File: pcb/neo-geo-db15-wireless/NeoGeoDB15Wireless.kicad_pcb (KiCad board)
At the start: 2 copper layers, 3 parts, among them J1 DB15_Female_MountingHoles, U1 RP2040-Zero, U2 NRF24L01_Breakout

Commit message: PCB schematic
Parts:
- U2: moved to B.Cu
- moved U2 29.5 mm to (113.0, 72.0), turned to 180 degrees
- moved J1 29.1 mm to (100.0, 92.8), turned to 180 degrees
- moved U1 19.5 mm to (104.6, 82.2), turned to 90 degrees
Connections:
- J1 pad 1: unconnected-(J1-Pad1) -> /GND
- J1 pad 11: unconnected-(J1-Pad11) -> /STA
- J1 pad 12: unconnected-(J1-Pad12) -> /BC
- J1 pad 13: unconnected-(J1-Pad13) -> /BA
- J1 pad 14: unconnected-(J1-Pad14) -> /DL
- J1 pad 15: unconnected-(J1-Pad15) -> /DU
- J1 pad 3: unconnected-(J1-Pad3) -> /SEL
- J1 pad 4: unconnected-(J1-Pad4) -> /BD
- J1 pad 5: unconnected-(J1-Pad5) -> /BB
- J1 pad 6: unconnected-(J1-Pad6) -> /DR
- J1 pad 7: unconnected-(J1-Pad7) -> /DD
- J1 pad 8: unconnected-(J1-Pad8) -> /VCC
- U1 pad 1: unconnected-(U1-Pad1) -> /DU
- U1 pad 10: unconnected-(U1-Pad10) -> /SEL
- U1 pad 13: unconnected-(U1-Pad13) -> /MISO
- U1 pad 14: unconnected-(U1-Pad14) -> /CS
- U1 pad 15: unconnected-(U1-Pad15) -> /SCK
- U1 pad 16: unconnected-(U1-Pad16) -> /MOSI
- U1 pad 17: unconnected-(U1-Pad17) -> /CE
- U1 pad 18: unconnected-(U1-Pad18) -> /IRQ
- U1 pad 19: Net-(U1-Pad19) -> unconnected-(U1-Pad19)
- U1 pad 2: unconnected-(U1-Pad2) -> /DD
- U1 pad 20: Net-(U1-Pad20) -> unconnected-(U1-Pad20)
- U1 pad 21: unconnected-(U1-Pad21) -> Net-(U1-Pad21)
- U1 pad 22: unconnected-(U1-Pad22) -> /VCC
- U1 pad 23: unconnected-(U1-Pad23) -> /GND
- U1 pad 3: unconnected-(U1-Pad3) -> /DL
- U1 pad 4: unconnected-(U1-Pad4) -> /DR
- U1 pad 5: unconnected-(U1-Pad5) -> /BA
- U1 pad 6: unconnected-(U1-Pad6) -> /BB
- U1 pad 7: unconnected-(U1-Pad7) -> /BC
- U1 pad 8: unconnected-(U1-Pad8) -> /BD
- U1 pad 9: unconnected-(U1-Pad9) -> /STA
- U2 pad 1: unconnected-(U2-Pad1) -> /GND
- U2 pad 2: unconnected-(U2-Pad2) -> Net-(U1-Pad21)
- U2 pad 3: Net-(U1-Pad20) -> /CE
- U2 pad 4: unconnected-(U2-Pad4) -> /CS
- U2 pad 5: unconnected-(U2-Pad5) -> /SCK
- U2 pad 6: unconnected-(U2-Pad6) -> /MOSI
- U2 pad 7: unconnected-(U2-Pad7) -> /MISO
- U2 pad 8: Net-(U1-Pad19) -> /IRQ
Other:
- board outline added: 40 x 41 mm

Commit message: Routing
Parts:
- moved U2 0.71 mm to (112.5, 72.5), turned to 0 degrees
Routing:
- net /IRQ: track 0.00 -> 40.6 mm
- net /MOSI: track 0.00 -> 32.6 mm
- net /BC: track 0.00 -> 31.0 mm
- net /STA: track 0.00 -> 29.3 mm
- net /DU: track 0.00 -> 28.2 mm
- net /DD: track 0.00 -> 27.9 mm
- net Net-(U1-Pad21): track 0.00 -> 27.8 mm
- net /BD: track 0.00 -> 26.8 mm
- net /DL: track 0.00 -> 26.6 mm
- net /BA: track 0.00 -> 26.5 mm
- net /BB: track 0.00 -> 24.1 mm
- net /SCK: track 0.00 -> 23.6 mm
- net /CE: track 0.00 -> 23.3 mm
- net /DR: track 0.00 -> 23.3 mm
- net /SEL: track 0.00 -> 22.4 mm
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- added copper zone on B.Cu, net /GND
- added copper zone on F.Cu, net /GND

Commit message: Making the right size
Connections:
- net Net-(U1-Pad21) renamed /3V3
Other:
- board size 40 x 41 mm -> 39.9 x 29.2 mm
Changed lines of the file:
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@@
       (outputformat 1)
       (mirror false)
-      (drillshape 1)
+      (drillshape 0)
       (scaleselection 1)
-      (outputdirectory "")
+      (outputdirectory "Gerbers/")
     )
   )
@@
   (net 22 "unconnected-(U1-Pad19)")
   (net 23 "unconnected-(U1-Pad20)")
-  (net 24 "Net-(U1-Pad21)")
+  (net 24 "/3V3")
   (net 25 "unconnected-(U1-Pad11)")
   (net 26 "unconnected-(U1-Pad12)")
@@
       (effects (font (size 1 1) (thickness 0.15)))
     )
-    (fp_line (start 19.16 -0.95) (end 19.16 -24.45) (layer "F.SilkS") (width 0.12))
-    (fp_line (start 1.16 -0.95) (end 19.16 -0.95) (layer "F.SilkS") (width 0.12))
-    (fp_line (start 19.16 -24.45) (end 1.16 -24.45) (layer "F.SilkS") (width 0.12))
-    (fp_line (start 1.16 -24.45) (end 1.16 -0.95) (layer "F.SilkS") (width 0.12))
     (fp_line (start 1.16 -0.95) (end 1.16 -24.45) (layer "F.CrtYd") (width 0.05))
     (fp_line (start 19.16 -0.95) (end 1.16 -0.95) (layer "F.CrtYd") (width 0.05))
@@
       (net 23 "unconnected-(U1-Pad20)") (pinfunction "GP29") (pintype "bidirectional+no_connect"))
     (pad "21" thru_hole roundrect (at 2.54 -17.78 90) (size 2.6 1.6002) (drill 0.8 (offset -0.6 0)) (layers *.Cu *.Mask) (roundrect_rratio 0.25)
-      (net 24 "Net-(U1-Pad21)") (pinfunction "3V3") (pintype "power_in"))
+      (net 24 "/3V3") (pinfunction "3V3") (pintype "power_in"))
     (pad "22" thru_hole roundrect (at 2.54 -12.7 90) (size 2.6 1.6002) (drill 0.8 (offset -0.6 0)) (layers *.Cu *.Mask) (roundrect_rratio 0.25)
       (net 3 "/VCC") (pinfunction "5V") (pintype "power_in"))
@@
     (property "Sheetname" "")
     (attr through_hole)
-    (fp_text reference "J1" (at -21.1709 8.1408 180) (layer "F.SilkS")
+    (fp_text reference "J1" (at 0.8 0.25 180) (layer "F.SilkS") hide
       (effects (font (size 1 1) (thickness 0.15)) (justify left))
     )
@@
       (effects (font (size 1.27 1.27) (thickness 0.15)))
     )
-    (fp_text user "Connector out this way" (at 0 -6 unlocked) (layer "F.SilkS")
-      (effects (font (size 1 1) (thickness 0.15)))
-    )
-    (fp_line (start 19.7612 9.5885) (end 19.7612 -9.5885) (layer "F.SilkS") (width 0.15))
-    (fp_line (start -19.7612 9.5885) (end 19.7612 9.5885) (layer "F.SilkS") (width 0.15))
-    (fp_line (start -19.7612 9.5885) (end -19.7612 -9.5885) (layer "F.SilkS") (width 0.15))
-    (fp_line (start -19.7612 -9.5885) (end 19.7612 -9.5885) (layer "F.SilkS") (width 0.15))
-    (fp_rect (start -16 -9.5885) (end 16 -2) (layer "F.SilkS") (width 0.12) (fill none))
-    (fp_poly (pts
-        (xy 1 -8)
-        (xy -1 -8)
-        (xy 0 -9)
-      ) (layer "F.SilkS") (width 0.12) (fill solid))
     (fp_line (start -19.7862 9.6135) (end 19.7862 9.6135) (layer "F.CrtYd") (width 0.15))
     (fp_line (start 19.7862 9.6135) (end 19.7862 -9.6135) (layer "F.CrtYd") (width 0.15))
@@
     (fp_line (start -19.7612 -9.5885) (end 19.7612 -9.5885) (layer "F.Fab") (width 0.15))
     (fp_line (start -19.7612 9.5885) (end -19.7612 -9.5885) (layer "F.Fab") (width 0.15))
-    (pad "" np_thru_hole circle (at -16.6624 6.2992 180) (size 4.825 4.825) (drill 3.175) (layers F&B.Cu *.Mask)
-      (pinfunction "PAD") (pintype "passive+no_connect"))
-    (pad "" np_thru_hole circle (at 16.6624 6.2992 180) (size 4.825 4.825) (drill 3.175) (layers F&B.Cu *.Mask)
-      (pinfunction "PAD") (pintype "passive+no_connect"))
+    (pad "" np_thru_hole circle (at -16.6624 6.2992 180) (size 4.825 4.825) (drill 3.175) (layers F&B.Cu *.Mask))
+    (pad "" np_thru_hole circle (at 16.6624 6.2992 180) (size 4.825 4.825) (drill 3.175) (layers F&B.Cu *.Mask))
     (pad "1" thru_hole circle (at -9.601192 7.7216 180) (size 1.591397 1.591397) (drill 1.0414) (layers *.Cu *.Mask)
       (net 10 "/GND") (pinfunction "1") (pintype "passive"))
@@
       (net 10 "/GND") (pinfunction "GND") (pintype "power_in"))
     (pad "2" smd rect (at -4.4 -8.7) (size 1 2) (layers "B.Cu" "B.Paste" "B.Mask")
-      (net 24 "Net-(U1-Pad21)") (pinfunction "VCC") (pintype "power_in"))
+      (net 24 "/3V3") (pinfunction "VCC") (pintype "power_in"))
     (pad "3" smd rect (at -1.86 -8.7) (size 1 2) (layers "B.Cu" "B.Paste" "B.Mask")
       (net 20 "/CE") (pinfunction "CE") (pintype "input"))
@@
     )
   )
-  (gr_rect (start 80 102.5) (end 120 61.5) (layer "Edge.Cuts") (width 0.1) (fill none))
+  (gr_rect (start 80 90.7) (end 119.9 61.5) (layer "Edge.Cuts") (width 0.1) (fill none))
   (segment (start 90.398799 85.0284) (end 91.925 83.502199) (width 0.4) (layer "F.Cu") (net 3))
   (segment (start 91.925 83.502199) (end 91.925 79.675) (width 0.4) (layer "F.Cu") (net 3))
@@
   (segment (start 97.25 83.25) (end 94.465 80.465) (width 0.25) (layer "B.Cu") (net 21))
   (segment (start 111.25 83.25) (end 97.25 83.25) (width 0.25) (layer "B.Cu") (net 21))
-  (segment (start 101.06 65.46) (end 86.845 79.675) (width 0.25) (layer "B.Cu") (net 24))
-  (segment (start 106.44 65.46) (end 101.06 65.46) (width 0.25) (layer "B.Cu") (net 24))
-  (segment (start 108.1 63.8) (end 106.44 65.46) (width 0.25) (layer "B.Cu") (net 24))
+  (segment (start 106.3 65.6) (end 108.1 63.8) (width 0.4) (layer "B.Cu") (net 24))
+  (segment (start 86.845 79.655) (end 100.9 65.6) (width 0.4) (layer "B.Cu") (net 24))
+  (segment (start 86.845 79.675) (end 86.845 79.655) (width 0.4) (layer "B.Cu") (net 24))
+  (segment (start 100.9 65.6) (end 106.3 65.6) (width 0.4) (layer "B.Cu") (net 24))
   (zone (net 10) (net_name "/GND") (layers F&B.Cu) (hatch edge 0.508)
     (connect_pads (clearance 0.508))

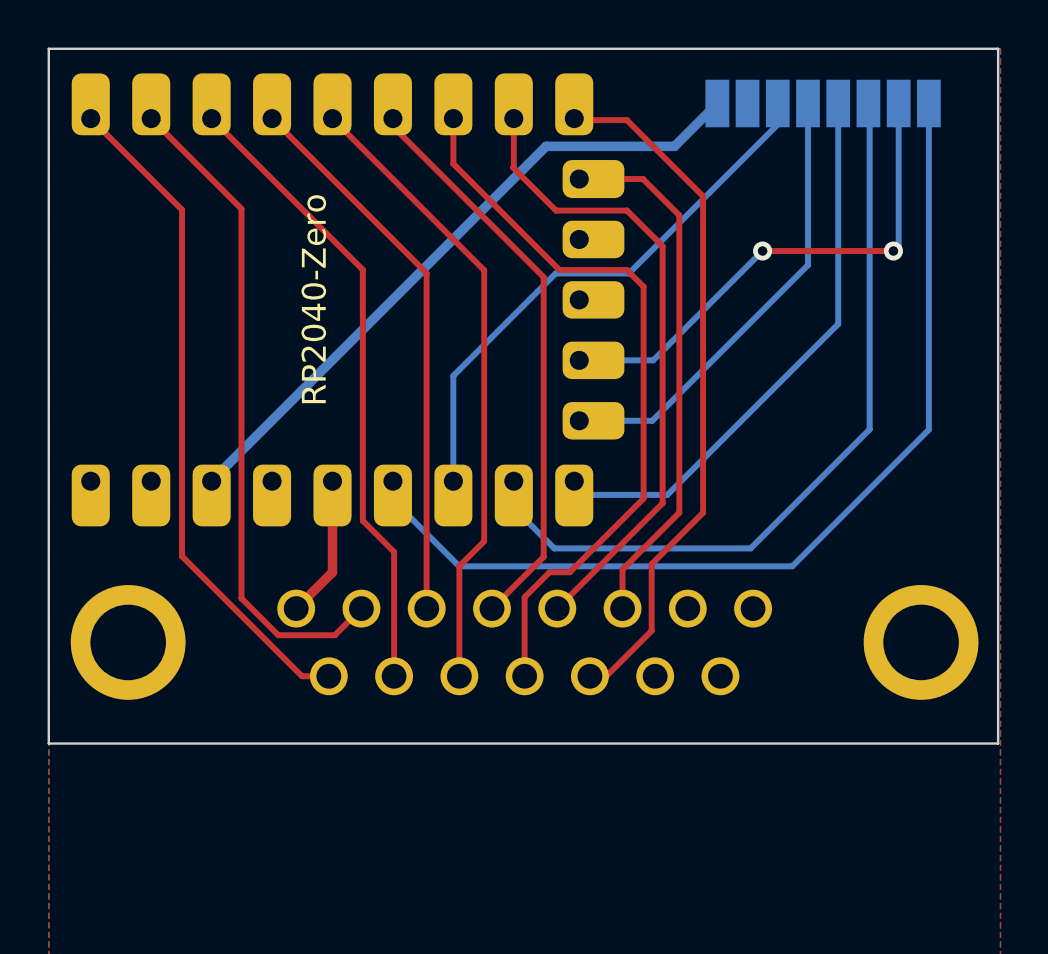
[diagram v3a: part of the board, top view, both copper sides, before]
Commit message: Correct size, add some silkscreen
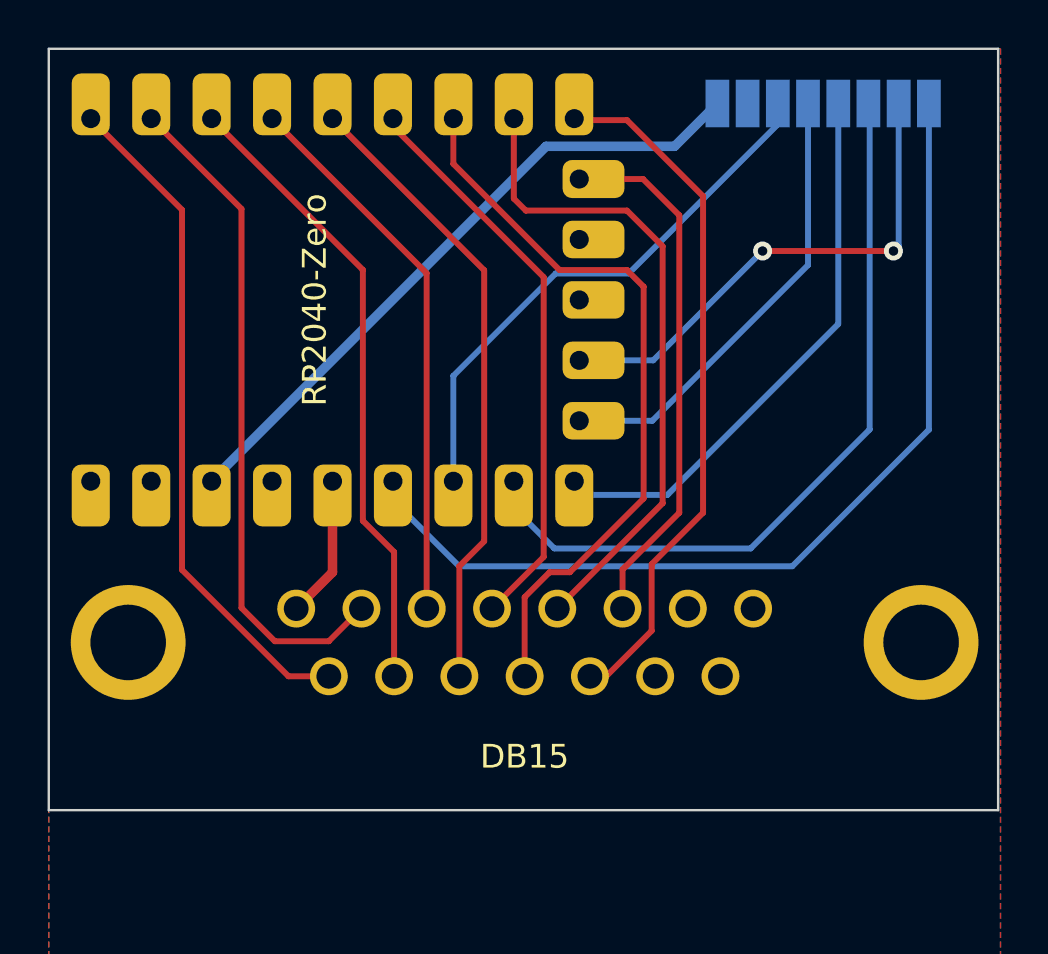
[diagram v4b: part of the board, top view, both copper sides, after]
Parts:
- U2: value NRF24L01_Breakout -> NRF24L01
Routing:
- net /BD: track 26.8 -> 27.5 mm
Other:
- board size 39.9 x 29.2 mm -> 39.9 x 32 mm
- board text added: "DB15"
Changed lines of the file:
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@@
     (property "Sheetname" "")
     (attr through_hole)
-    (fp_text reference "U2" (at 0 -1.1 180) (layer "B.SilkS")
+    (fp_text reference "U2" (at 0 -1.1 180) (layer "B.Fab")
       (effects (font (size 1 1) (thickness 0.15)) (justify mirror))
     )
-    (fp_text value "NRF24L01_Breakout" (at 0 4.8 180) (layer "B.Fab")
+    (fp_text value "NRF24L01" (at 0 7.75 180 unlocked) (layer "B.SilkS")
       (effects (font (size 1 1) (thickness 0.15)) (justify mirror))
     )
@@
     )
   )
-  (gr_rect (start 80 90.7) (end 119.9 61.5) (layer "Edge.Cuts") (width 0.1) (fill none))
+  (gr_rect (start 118.5 62.25) (end 106.5 81.75) (layer "B.SilkS") (width 0.15) (fill none))
+  (gr_rect (start 80 93.5) (end 119.9 61.5) (layer "Edge.Cuts") (width 0.1) (fill none))
+  (gr_text "DB15" (at 100 91.25) (layer "F.SilkS")
+    (effects (font (size 1 1) (thickness 0.15)))
+  )
   (segment (start 90.398799 85.0284) (end 91.925 83.502199) (width 0.4) (layer "F.Cu") (net 3))
   (segment (start 91.925 83.502199) (end 91.925 79.675) (width 0.4) (layer "F.Cu") (net 3))
-  (segment (start 88.1 84.6) (end 88.1 68.23) (width 0.25) (layer "F.Cu") (net 4))
-  (segment (start 93.141998 85.0284) (end 92.0213 86.149098) (width 0.25) (layer "F.Cu") (net 4))
-  (segment (start 92.0213 86.149098) (end 89.649098 86.149098) (width 0.25) (layer "F.Cu") (net 4))
   (segment (start 88.1 68.23) (end 84.305 64.435) (width 0.25) (layer "F.Cu") (net 4))
-  (segment (start 89.649098 86.149098) (end 88.1 84.6) (width 0.25) (layer "F.Cu") (net 4))
+  (segment (start 93.141998 85.0284) (end 91.770398 86.4) (width 0.25) (layer "F.Cu") (net 4))
+  (segment (start 89.5 86.4) (end 88.1 85) (width 0.25) (layer "F.Cu") (net 4))
+  (segment (start 91.770398 86.4) (end 89.5 86.4) (width 0.25) (layer "F.Cu") (net 4))
+  (segment (start 88.1 85) (end 88.1 68.23) (width 0.25) (layer "F.Cu") (net 4))
   (segment (start 95.8799 85.023103) (end 95.8799 70.9299) (width 0.25) (layer "F.Cu") (net 5))
   (segment (start 95.885197 85.0284) (end 95.8799 85.023103) (width 0.25) (layer "F.Cu") (net 5))
@@
   (segment (start 100.8 82.856796) (end 100.8 71.1) (width 0.25) (layer "F.Cu") (net 6))
   (segment (start 94.465 64.765) (end 94.465 64.435) (width 0.25) (layer "F.Cu") (net 6))
-  (segment (start 99.545 66.473602) (end 99.518602 66.5) (width 0.25) (layer "F.Cu") (net 7))
+  (segment (start 99.545 67.795) (end 100.05 68.3) (width 0.25) (layer "F.Cu") (net 7))
+  (segment (start 104.3 68.3) (end 105.8 69.8) (width 0.25) (layer "F.Cu") (net 7))
+  (segment (start 100.05 68.3) (end 104.3 68.3) (width 0.25) (layer "F.Cu") (net 7))
   (segment (start 105.8 69.8) (end 105.8 80.599995) (width 0.25) (layer "F.Cu") (net 7))
   (segment (start 105.8 80.599995) (end 101.371595 85.0284) (width 0.25) (layer "F.Cu") (net 7))
-  (segment (start 101.318602 68.3) (end 104.3 68.3) (width 0.25) (layer "F.Cu") (net 7))
-  (segment (start 104.3 68.3) (end 105.8 69.8) (width 0.25) (layer "F.Cu") (net 7))
-  (segment (start 99.518602 66.5) (end 101.318602 68.3) (width 0.25) (layer "F.Cu") (net 7))
-  (segment (start 99.545 64.435) (end 99.545 66.473602) (width 0.25) (layer "F.Cu") (net 7))
+  (segment (start 99.545 64.435) (end 99.545 67.795) (width 0.25) (layer "F.Cu") (net 7))
   (segment (start 104.114794 83.385206) (end 106.5 81) (width 0.25) (layer "F.Cu") (net 8))
   (segment (start 104.114794 85.0284) (end 104.114794 83.385206) (width 0.25) (layer "F.Cu") (net 8))
@@
   (segment (start 106.5 81) (end 106.5 68.5) (width 0.25) (layer "F.Cu") (net 8))
   (segment (start 106.5 68.5) (end 104.975 66.975) (width 0.25) (layer "F.Cu") (net 8))
-  (segment (start 85.6 82.82808) (end 85.6 68.27) (width 0.25) (layer "F.Cu") (net 11))
-  (segment (start 90.64512 87.8732) (end 85.6 82.82808) (width 0.25) (layer "F.Cu") (net 11))
+  (segment (start 91.770406 87.8732) (end 90.0732 87.8732) (width 0.25) (layer "F.Cu") (net 11))
   (segment (start 85.6 68.27) (end 81.765 64.435) (width 0.25) (layer "F.Cu") (net 11))
-  (segment (start 91.770406 87.8732) (end 90.64512 87.8732) (width 0.25) (layer "F.Cu") (net 11))
+  (segment (start 85.6 83.4) (end 85.6 68.27) (width 0.25) (layer "F.Cu") (net 11))
+  (segment (start 90.0732 87.8732) (end 85.6 83.4) (width 0.25) (layer "F.Cu") (net 11))
   (segment (start 93.2 70.79) (end 86.845 64.435) (width 0.25) (layer "F.Cu") (net 12))
   (segment (start 94.513605 87.8732) (end 94.513605 82.648981) (width 0.25) (layer "F.Cu") (net 12))
